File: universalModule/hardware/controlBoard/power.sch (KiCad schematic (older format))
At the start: 55 parts, among them U1 MP3431, U2 MP3431, U3 MP1496

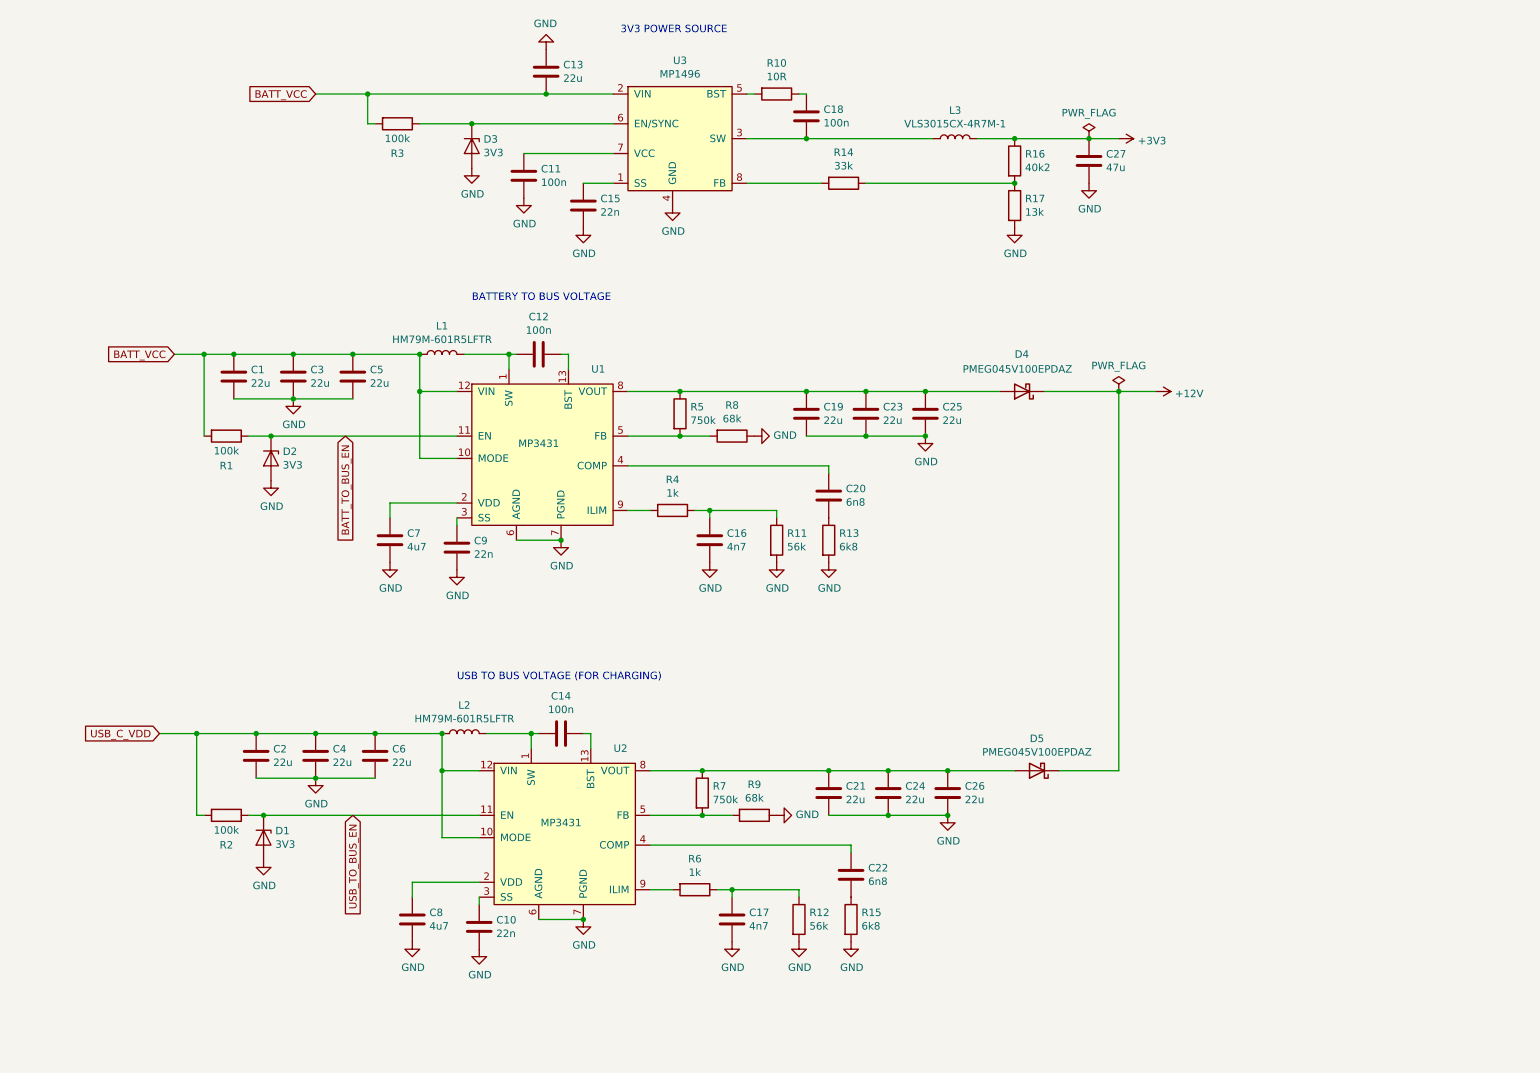
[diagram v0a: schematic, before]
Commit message: universalModule: Route the control boards
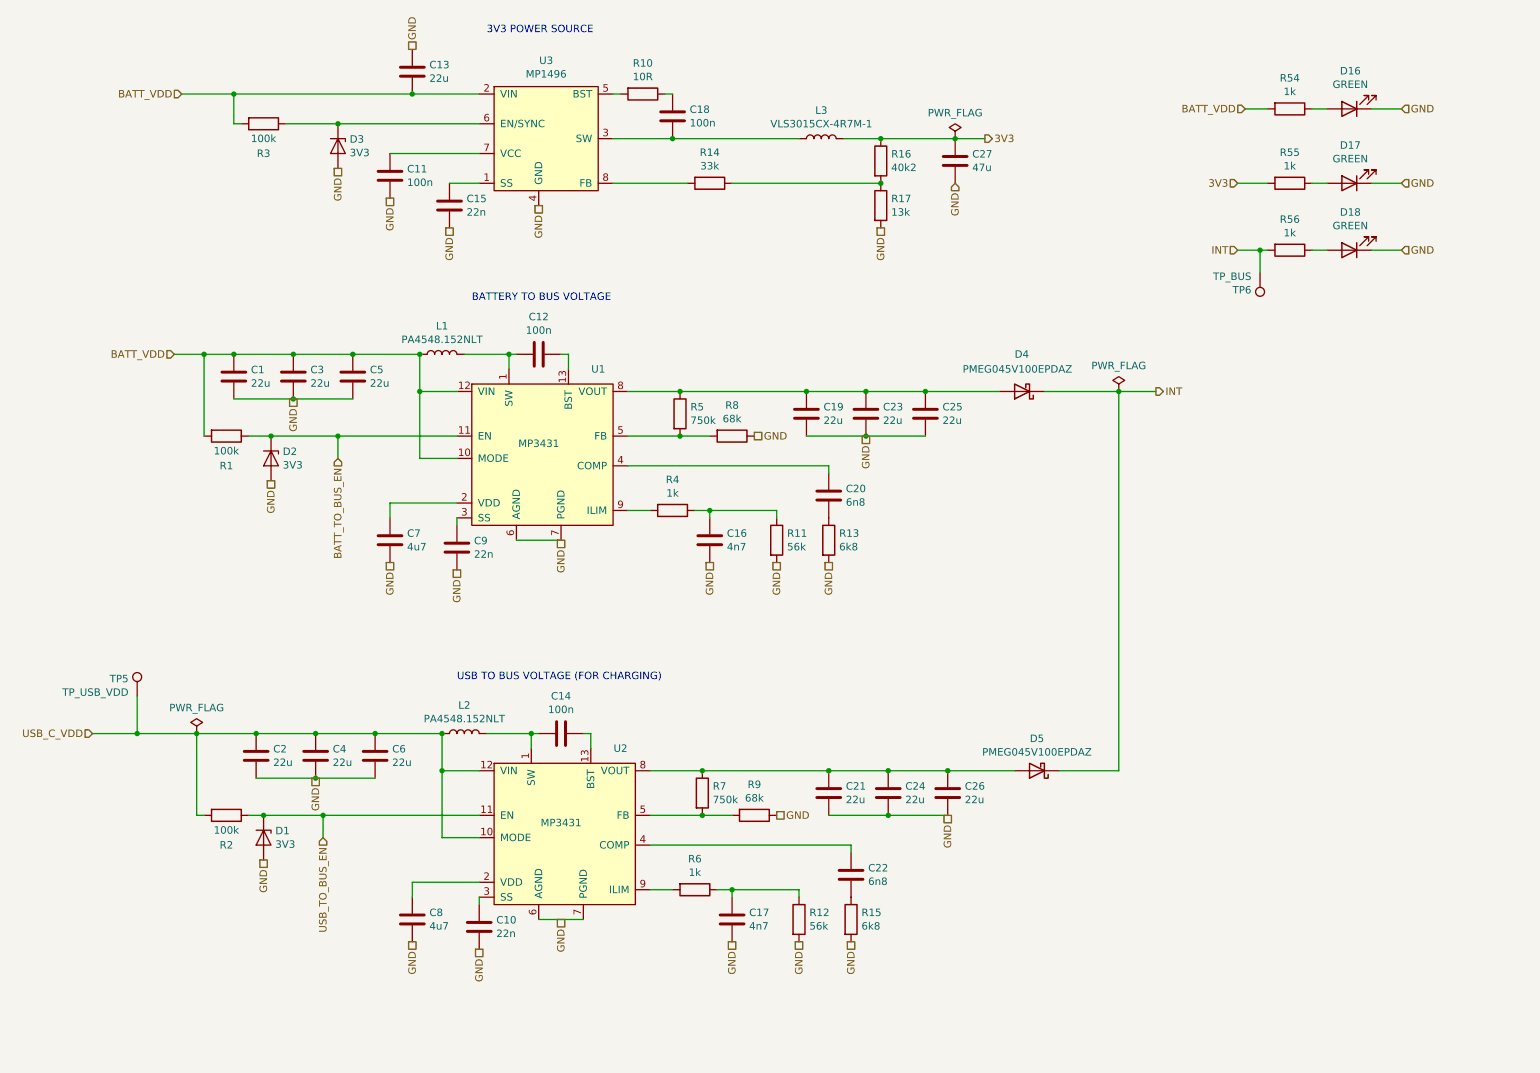
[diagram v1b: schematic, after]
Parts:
- added D16, D17, D18: GREEN, LED_SMD:LED_0603_1608Metric, symbol Device:LED
- added R54, R55, R56: 1k, Resistor_SMD:R_0402_1005Metric, symbol Device:R
- added TP5: TP_USB_VDD, TestPoint:TestPoint_Pad_D2.0mm, symbol Connector:TestPoint
- added TP6: TP_BUS, TestPoint:TestPoint_Pad_D2.0mm, symbol Connector:TestPoint
- D4, D5: #manf (none) -> PMEG045V100EPDAZ
- L1, L2: value HM79M-601R5LFTR -> PA4548.152NLT; footprint rofi:HM79M-60 -> rofi:PA4548; #manf HM79M-601R5LFTR -> PA4548.152NLT
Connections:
- net GND: now also D16.1 (K), D17.1 (K), D18.1 (K)
- net USB_C_VDD: now also TP5.1
- net +12V renamed INT
- net INT: now also R56.2, TP6.1
- net +3V3 renamed 3V3
- net 3V3: now also R55.2
- net BATT_VCC renamed BATT_VDD
- net BATT_VDD: now also R54.2
- new net: D18.2 (A), R56.1
- new net: D17.2 (A), R55.1
- new net: D16.2 (A), R54.1
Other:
- moved on the sheet: C11, C13, C15, C18, C27, D3, L3, R10, R14, R16, R17, R3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

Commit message: UniversalModule: Start version 2
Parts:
- removed C1, C13, C19, C2, C21, C23, C24, C25, C26, C3, C4, C5, C6: 22u, Capacitor_SMD:C_0805_2012Metric, symbol Device:C
- removed C10, C15, C9: 22n, Capacitor_SMD:C_0402_1005Metric, symbol Device:C
- removed C11, C12, C14: 100n, Capacitor_SMD:C_0402_1005Metric, symbol Device:C
- removed C16, C17: 4n7, Capacitor_SMD:C_0402_1005Metric, symbol Device:C
- removed C20, C22: 6n8, Capacitor_SMD:C_0402_1005Metric, symbol Device:C
- removed C27: 47u, Capacitor_SMD:C_0805_2012Metric, symbol Device:C
- removed C7, C8: 4u7, Capacitor_SMD:C_0402_1005Metric, symbol Device:C
- removed D1, D2, D3: 3V3, Diode_SMD:D_SOD-323, symbol Device:D_Zener
- removed D4, D5: PMEG045V100EPDAZ, rofi:D_SOT1289, symbol Device:D_Schottky
- removed L1, L2: PA4548.152NLT, rofi:PA4548, symbol Device:L
- removed L3: VLS3015CX-4R7M-1, rofi:VLS3015CX-1, symbol Device:L
- removed R1, R2, R3: 100k, Resistor_SMD:R_0402_1005Metric, symbol Device:R
- removed R10: 10R, Resistor_SMD:R_0402_1005Metric, symbol Device:R
- removed R11, R12: 56k, Resistor_SMD:R_0402_1005Metric, symbol Device:R
- removed R13, R15: 6k8, Resistor_SMD:R_0402_1005Metric, symbol Device:R
- removed R14: 33k, Resistor_SMD:R_0402_1005Metric, symbol Device:R
- removed R16: 40k2, Resistor_SMD:R_0402_1005Metric, symbol Device:R
- removed R17: 13k, Resistor_SMD:R_0402_1005Metric, symbol Device:R
- removed R4, R54, R6: 1k, Resistor_SMD:R_0402_1005Metric, symbol Device:R
- removed R5, R7: 750k, Resistor_SMD:R_0402_1005Metric, symbol Device:R
- removed R8, R9: 68k, Resistor_SMD:R_0402_1005Metric, symbol Device:R
- removed TP5: TP_USB_VDD, TestPoint:TestPoint_Pad_D2.0mm, symbol Connector:TestPoint
- removed U1, U2: MP3431, rofi:QFN-13, symbol rofi:MP3431
- removed U3: MP1496, Package_TO_SOT_SMD:TSOT-23-8, symbol rofi:MP1496
- added C? (x22): 22u, Capacitor_SMD:C_0805_2012Metric, symbol Device:C
- added C? (x4): 100n, Capacitor_SMD:C_0603_1608Metric, symbol Device:C
- added C? (x2): 2u2, Capacitor_SMD:C_0603_1608Metric, symbol Device:C
- added C? (x2): 1u, Capacitor_SMD:C_0603_1608Metric, symbol Device:C
- added C? (x2): 27p, Capacitor_SMD:C_0402_1005Metric, symbol Device:C
- added C? (x2): 470p, Capacitor_SMD:C_0402_1005Metric, symbol Device:C
- added C? (x2): 22n, Capacitor_SMD:C_0402_1005Metric, symbol Device:C
- added D? (x2): SB1045L, Package_TO_SOT_SMD:TO-277B, symbol Device:D_AAK
- added L? (x2): 1u5/2u2, rofi:MGV1004, symbol Device:L
- added L?: 4u7, rofi:SMNR5020, symbol Device:L
- added R? (x2): 150k, Capacitor_SMD:C_0402_1005Metric, symbol Device:R
- added R? (x2): 510k, Resistor_SMD:R_0402_1005Metric, symbol Device:R
- added R? (x2): 56k, Resistor_SMD:R_0402_1005Metric, symbol Device:R
- added R? (x2): 75k, symbol Device:R
- added R? (x2): 0R, Resistor_SMD:R_0402_1005Metric, symbol Device:R
- added R? (x2): 47k, Resistor_SMD:R_0402_1005Metric, symbol Device:R
- added R?: 10k, symbol Device:R
- added R? (x2): 200k, Resistor_SMD:R_0402_1005Metric, symbol Device:R
- added R?: 44k2, Resistor_SMD:R_0402_1005Metric, symbol Device:R
- added R?: 10k, Resistor_SMD:R_0402_1005Metric, symbol Device:R
- added U? (x2): TPS61088, rofi:VFQFN-20-4.5mmx3.5mm, symbol rofi:TPS61088
- added U?: SY8105, Package_TO_SOT_SMD:TSOT-23-6, symbol rofi:SY8105
- C18: footprint Capacitor_SMD:C_0402_1005Metric -> Capacitor_SMD:C_0603_1608Metric; #manf 885012105016 -> (none); LCSC (none) -> C14663
- D16, D17, D18: LCSC (none) -> C72043
- R55: #manf RR0510P-102-D -> (none); LCSC (none) -> C11702
- R56: value 1k -> 10k; #manf RR0510P-102-D -> (none); LCSC (none) -> C25744
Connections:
- net 3V3: now also C?.1, C?.1, C?.1, L?.2, R?.1
- net BATT_TO_BUS_EN: now also U?.2 (EN)
- net BATT_VDD: now also C?.1, C?.1, C?.1, C?.1, C?.1, C?.1, C?.1, C?.1, L?.2, R?.1, R?.2, U?.4 (IN), U?.9 (VIN)
- net GND: now also C?.2, C?.2, C?.2, C?.2, C?.2, C?.2, C?.2, C?.2, C?.2, C?.2, C?.2, C?.2, C?.2, C?.2, C?.2, C?.2, C?.2, C?.2, C?.2, C?.2, C?.2, C?.2, C?.2, C?.2, R?.2, R?.2, R?.2, R?.2, R?.2, R?.2, R?.2, U?.11 (NC), U?.11 (NC), U?.12 (NC), U?.12 (NC), U?.20 (AGND), U?.20 (AGND), U?.21 (PGND), U?.21 (PGND), U?.3 (GND)
- net INT: now also D?.3 (K), D?.3 (K)
- net USB_C_VDD: now also C?.1, C?.1, C?.1, C?.1, C?.1, L?.2, U?.9 (VIN)
- net USB_TO_BUS_EN: now also R?.2, U?.2 (EN)
- net at C18.2: now also L?.1, U?.5 (LX)
- net at C18.1: now also U?.6 (BS)
- net at D16.2 (A): now also R?.1
- new net: C?.1, U?.1 (VCC)
- new net: C?.1, U?.10 (SS) (x2)
- new net: R?.1, U?.13 (MODE) (x2)
- new net: C?.1, C?.1, C?.1, C?.1, C?.1, D?.1 (A), D?.2 (A), R?.1, U?.14 (VOUT), U?.15 (VOUT), U?.16 (VOUT) (x2)
- new net: R?.1, R?.2, U?.17 (FB) (x2)
- new net: C?.1, R?.1, U?.18 (COMP) (x2)
- new net: R?.1, U?.19 (ILIM) (x2)
- new net: R?.1, U?.3 (FSW) (x2)
- new net: C?.2, L?.1, R?.2, U?.4 (SW), U?.5 (SW), U?.6 (SW), U?.7 (SW) (x2)
- new net: C?.1, U?.8 (BOOT) (x2)
- new net: C?.2, C?.2, C?.2, C?.2, C?.2 (x2)
- new net: C?.1, R?.2 (x2)
- new net: C?.1, R?.1, U?.1 (VCC)
- new net: R?.1, R?.2, U?.1 (FB)
- new net: R?.2, U?.2 (EN)
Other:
- moved on the sheet: C18, D16, D17, D18, R55, R56, TP6
